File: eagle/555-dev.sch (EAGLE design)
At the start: 25 parts, among them IC1 NE555, Q1 IRF740, T1 2N2222

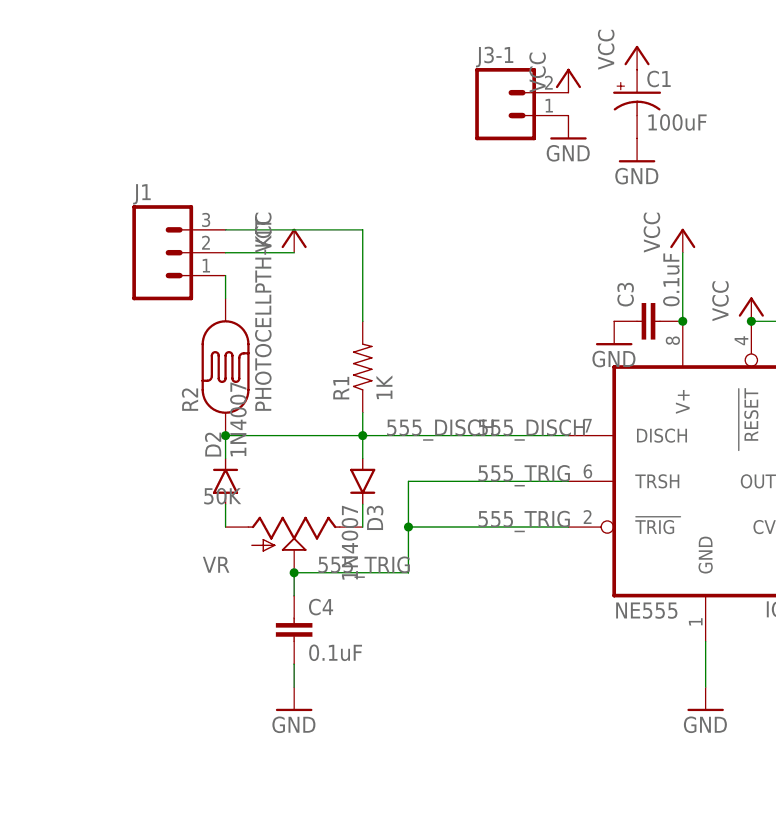
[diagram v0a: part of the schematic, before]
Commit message: add one more photoresistor and change the R network
user can use the PINS and VR(max/min) to stable the high pulse or the
low one
while the  frequency is modulated by photoresistors, duty cycle changes
due to the static pulse width
simulation: http://goo.gl/erNx82
Layout to be done
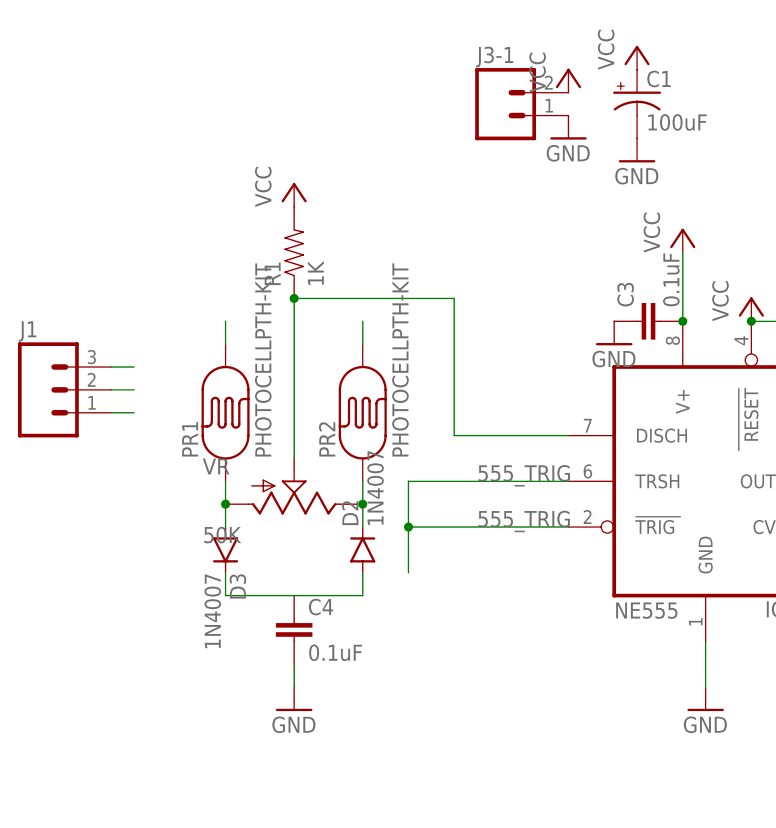
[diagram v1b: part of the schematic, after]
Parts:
- removed R2: PHOTOCELLPTH-KIT, SparkFun-Sensors:PHOTOCELLPTH-KIT
- added PR1, PR2: PHOTOCELLPTH-KIT, SparkFun-Sensors:PHOTOCELLPTH-KIT
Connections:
- removed net N$1: D3.C, VR.E
- removed net N$13: D2.A, VR.A
- new net N$4: C4.1, D2.A, D3.C
- new net PR1: J1.1, PR1.P$2
- new net PR2: J1.3, PR2.P$2
- net 555_DISCH: now also J1.2, VR.S; no longer D2.C, D3.A, R2.P$1
- net 555_TRIG: no longer C4.1, VR.S
- net N$2: now also D2.C, PR2.P$1, VR.E; no longer J1.1, R2.P$2
- net N$3: now also D3.A, PR1.P$1, VR.A; no longer J1.3, R1.2
- net VCC: now also R1.2; no longer J1.2
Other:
- moved on the sheet: D2, D3, J1, R1, VR

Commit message: added LOGO
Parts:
- added JP3: POWER_JACKPTH, SparkFun-Connectors:POWER_JACKPTH
- added U$1: LOGO, SparkFun-Electromechanical:LOGO
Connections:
- net GND: now also JP3.GND
- net VCC: now also JP3.PWR
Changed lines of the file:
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@@
 <?xml version="1.0" encoding="utf-8"?>
 <!DOCTYPE eagle SYSTEM "eagle.dtd">
-<eagle version="7.2.0">
+<eagle version="7.5.0">
 <drawing>
 <settings>
@@
 <part name="J1" library="SparkFun-Connectors" deviceset="M03" device="PTH"/>
 <part name="PR2" library="SparkFun-Sensors" deviceset="PHOTOCELL" device="PTH-KIT"/>
+<part name="JP3" library="SparkFun-Connectors" deviceset="POWER_JACK" device="PTH"/>
+<part name="P+2" library="supply1" deviceset="VCC" device=""/>
+<part name="GND3" library="supply1" deviceset="GND" device=""/>
+<part name="U$1" library="SparkFun-Electromechanical" deviceset="LOGO" device=""/>
 </parts>
 <sheets>
@@
 <instance part="J1" gate="J$1" x="20.32" y="50.8"/>
 <instance part="PR2" gate="G$1" x="55.88" y="48.26" rot="R90"/>
+<instance part="JP3" gate="G$1" x="109.22" y="76.2"/>
+<instance part="P+2" gate="VCC" x="111.76" y="86.36"/>
+<instance part="GND3" gate="1" x="111.76" y="76.2"/>
+<instance part="U$1" gate="G$1" x="33.02" y="86.36"/>
 </instances>
 <busses>
@@
 <pinref part="GND10" gate="1" pin="GND"/>
 </segment>
+<segment>
+<pinref part="JP3" gate="G$1" pin="GND"/>
+<pinref part="GND3" gate="1" pin="GND"/>
+</segment>
 </net>
 <net name="N$5" class="0">
@@
 <pinref part="R1" gate="G$1" pin="2"/>
 </segment>
-</net>
+<segment>
+<pinref part="JP3" gate="G$1" pin="PWR"/>
+<pinref part="P+2" gate="VCC" pin="VCC"/>
+</segment>
+</net>
